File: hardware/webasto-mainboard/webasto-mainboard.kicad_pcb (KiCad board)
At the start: 4 copper layers, 86.8 x 76 mm, 80 parts, among them J1 DEBUG, Q1 DMG2301L, Q10 2N7002, Q11 2N7002, Q12 SSM3J374R, Q13 2N7002, Q14 SUD50P04-08, Q15 SUD50P04-08, Q16 SUD50P04-08, Q17 SUD50P04-08, Q18 SUD50P04-08, Q2 2N7002, Q3 2N7002, Q4 2N7002, Q5 2N7002, Q6 SUD50P04-08, Q7 SUD50P04-08, Q8 SUD50P04-08, Q9 SUD50P04-08, U1 Pico, U2 LM4040DBZ-2.0, U3 LM7805_TO220, U4 MC33660BEFR2, U5 INA219BxDCN, U6 BD9G341EFJ

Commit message: Added logging, added debug serial to mainboard
- also added eeprom read support, and the digital GPIO over I2C
- route the ignition wire as a digital GPIO so we can use it as an input
  to the state machine.
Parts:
- added J1: Console FTDI, Beirdo:FTDI_BASIC, F.Cu at (124.7, 101.9)
- renumbered J1 to J2
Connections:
- U1 pad 24: unconnected-(U1-Pad24) -> ConsoleCTS
- U1 pad 25: unconnected-(U1-Pad25) -> ConsoleRTS
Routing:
- net ConsoleTX: track 0.00 -> 62.9 mm
- net ConsoleRX: track 0.00 -> 61.6 mm, vias 0 -> 1
- net ConsoleRTS: track 0.00 -> 39.8 mm, vias 0 -> 1
- net ConsoleCTS: track 0.00 -> 26.2 mm, vias 0 -> 1
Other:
- board text added: "Webasto Thermo Top C Replacement Controller"
- board text removed: "Webasto Therma Top C Replacement Controller"

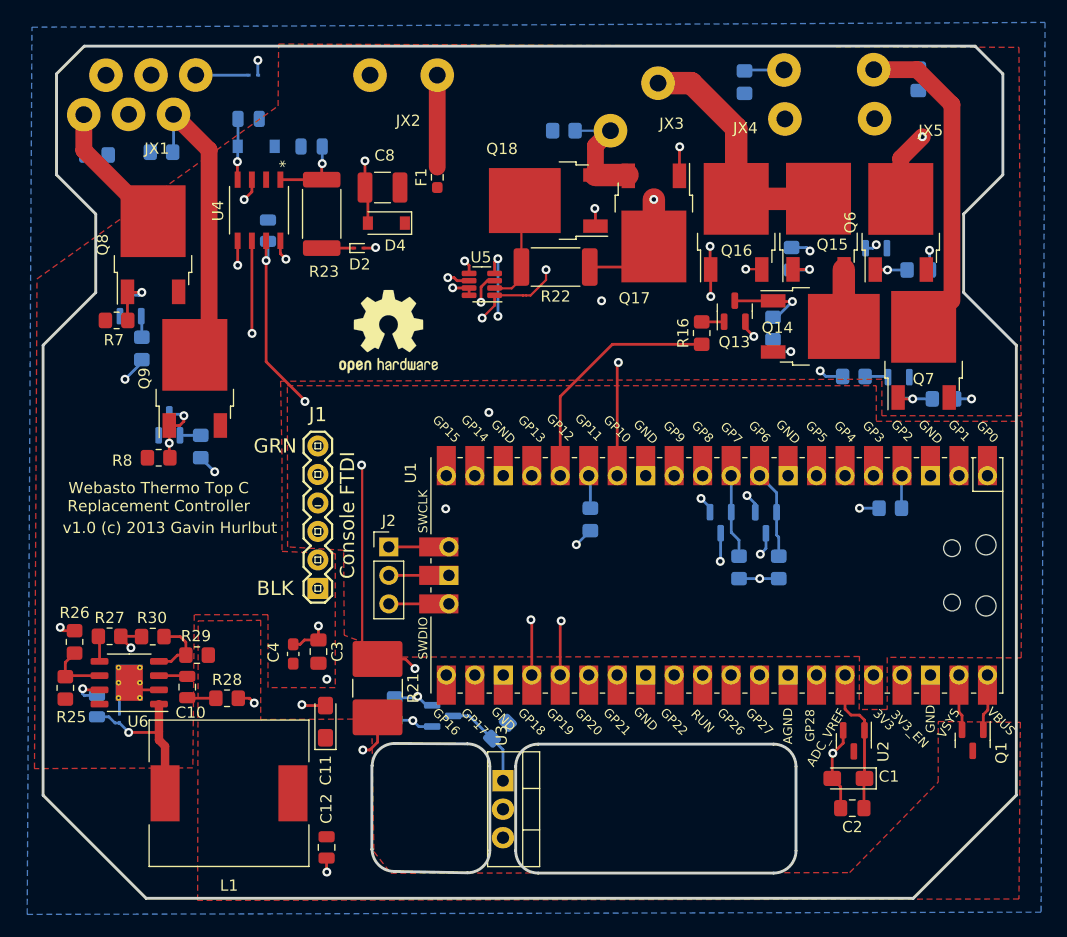
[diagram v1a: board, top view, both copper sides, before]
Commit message: Added a 4kbit FRAM on the mainboard to hold nonvolatile
- things like burn hours.
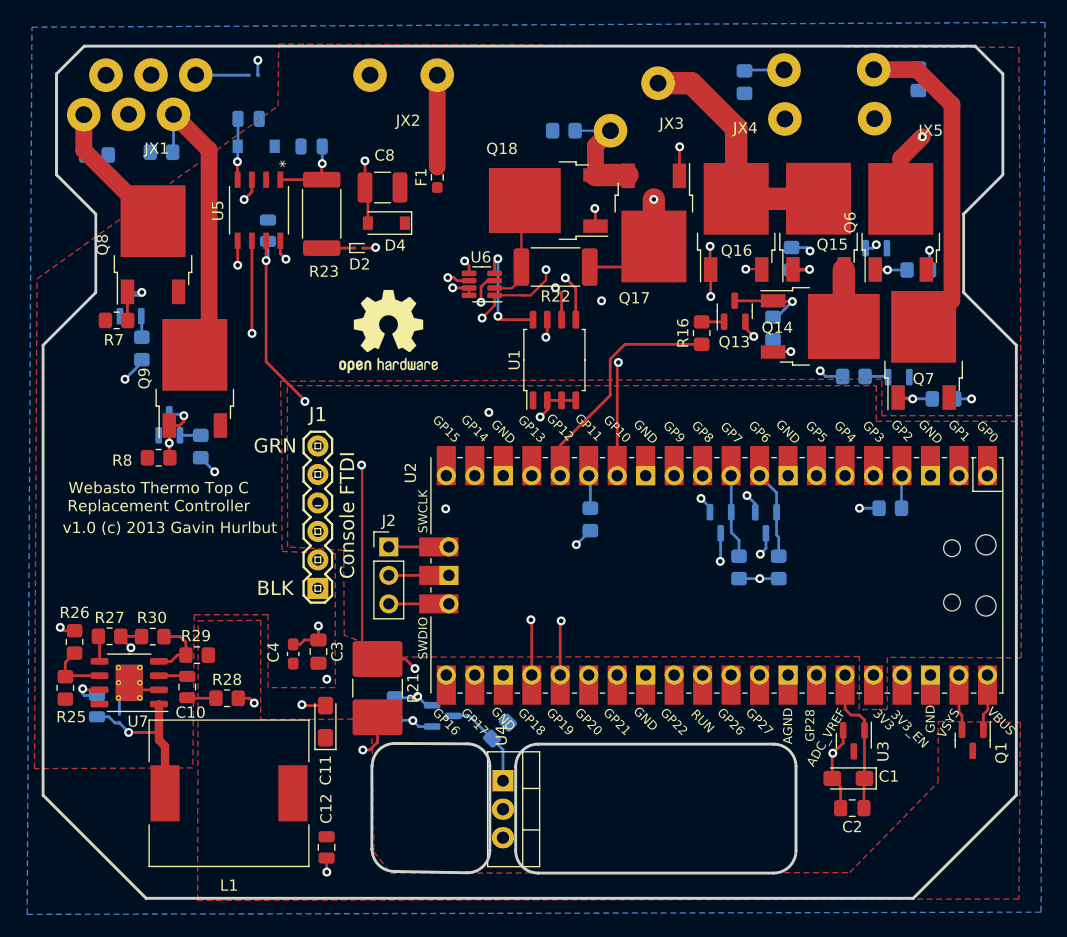
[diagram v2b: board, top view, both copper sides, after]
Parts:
- added U1: CY15E004J, Package_SO:SOIC-8_5.23x5.23mm_P1.27mm, F.Cu at (145.8, 81.5)
- renumbered U1 to U2, U2 to U3, U3 to U4, U4 to U5, U5 to U6, U6 to U7
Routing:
- net GND: track 53.5 -> 59.4 mm, vias 12 -> 14
- net SDA: track 80.6 -> 84.7 mm, vias 1 -> 2
- net +3V3: track 41.7 -> 44.9 mm
- net SCL: track 78.8 -> 81.9 mm, vias 2 -> 3
- net GlowPlugOut3V: track 21.6 -> 20.9 mm

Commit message: Added EmergencyStop input.  Hope I never need it.
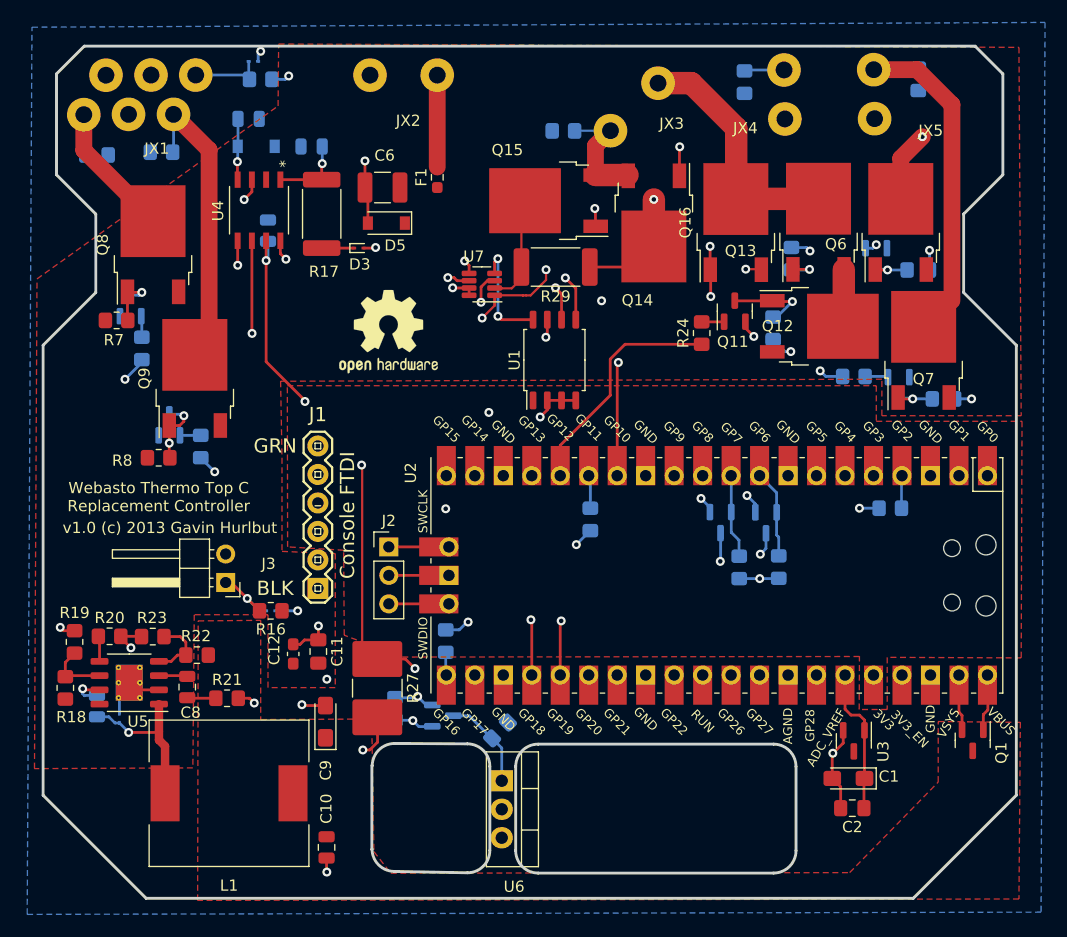
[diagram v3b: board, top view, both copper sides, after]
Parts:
- removed the C3 at (124.8, 107.5)
- removed the C4 at (122.5, 107.8)
- removed the R14 at (162.3, 100.0)
- removed the R17 at (131.6, 112.7)
- removed the R18 at (166.9, 72.5)
- removed the R19 at (140.9, 114.6)
- removed the R20 at (165.3, 78.7)
- removed the R21 at (130.0, 110.8)
- removed the R22 at (145.9, 73.2)
- removed the U4 at (141.2, 119.1)
- added C11: 100nF 25V, Capacitor_SMD:C_0805_2012Metric_Pad1.18x1.45mm_HandSolder, F.Cu at (124.7, 107.5)
- added C12: 100nF 25V, Capacitor_SMD:C_0603_1608Metric_Pad1.08x0.95mm_HandSolder, F.Cu at (122.5, 107.8)
- added D1: ACDBQC0130L-HF, Diode_SMD:D_SOD-923, B.Cu at (120.5, 103.9)
- added J3: 2-pole connector, Connector_PinHeader_2.54mm:PinHeader_1x02_P2.54mm_Horizontal, F.Cu at (116.5, 101.4)
- added R13: 10k, Resistor_SMD:R_0805_2012Metric_Pad1.20x1.40mm_HandSolder, B.Cu at (136.1, 106.6)
- added R25: 10k, Resistor_SMD:R_0805_2012Metric_Pad1.20x1.40mm_HandSolder, B.Cu at (140.9, 114.6)
- added R26: 10k, Resistor_SMD:R_0805_2012Metric_Pad1.20x1.40mm_HandSolder, B.Cu at (165.3, 78.7)
- added R27: 50R 1% 1W, Resistor_SMD:R_2816_7142Metric_Pad3.20x4.45mm_HandSolder, F.Cu at (130.0, 110.8)
- added R28: 100k, Resistor_SMD:R_0805_2012Metric_Pad1.20x1.40mm_HandSolder, B.Cu at (146.6, 61.1)
- added R29: 1R 1% 2W, Resistor_SMD:R_2512_6332Metric_Pad1.40x3.35mm_HandSolder, F.Cu at (145.9, 73.2)
- added R30: 10k, Resistor_SMD:R_0805_2012Metric_Pad1.20x1.40mm_HandSolder, B.Cu at (162.3, 100.0)
- added R31: 10k, Resistor_SMD:R_0805_2012Metric_Pad1.20x1.40mm_HandSolder, B.Cu at (165.8, 100.0)
- added R32: 10k, Resistor_SMD:R_0805_2012Metric_Pad1.20x1.40mm_HandSolder, B.Cu at (131.6, 112.6)
- added R33: 10k, Resistor_SMD:R_0805_2012Metric_Pad1.20x1.40mm_HandSolder, B.Cu at (166.9, 72.5)
- added U7: INA219BxDCN, Package_TO_SOT_SMD:SOT-23-8, F.Cu at (139.3, 74.8)
- Q10: value 2N7002 -> SSM3J374R
- Q11: moved to F.Cu
- Q12: value SSM3J374R -> SUD50P04-08; footprint Package_TO_SOT_SMD:SOT-23 -> Package_TO_SOT_SMD:TO-252-2; moved to F.Cu
- Q13: value 2N7002 -> SUD50P04-08; footprint Package_TO_SOT_SMD:SOT-23 -> Package_TO_SOT_SMD:TO-252-2
- Q17, Q18: value SUD50P04-08 -> 2N7002; footprint Package_TO_SOT_SMD:TO-252-2 -> Package_TO_SOT_SMD:SOT-23; moved to B.Cu
- R16: value 10R -> 10k
- R24: value 100k -> 10R; moved to F.Cu
- U6: value INA219BxDCN -> LM7805_TO220; footprint Package_TO_SOT_SMD:SOT-23-8 -> Package_TO_SOT_THT:TO-220-3_Vertical
- moved R15 63.5 mm to (119.6, 56.5), turned to 180 degrees
- moved Q12 48.3 mm to (169.4, 78.5)
- moved R16 45.7 mm to (120.5, 103.9), turned to 180 degrees
- moved U6 44.3 mm to (141.1, 119.1), turned to -90 degrees
- moved Q18 34.7 mm to (164.7, 96.1), turned to -90 degrees
- moved Q10 30.2 mm to (135.8, 113.2), turned to 0 degrees
- moved Q17 27.4 mm to (160.6, 96.0)
- moved Q15 24.2 mm to (145.3, 67.3), turned to 180 degrees
- moved R24 21.8 mm to (158.9, 79.1), turned to 90 degrees
- moved Q11 19.1 mm to (161.9, 77.2), turned to 90 degrees
- moved Q14 17.5 mm to (154.7, 69.3), turned to -90 degrees
- moved Q13 10.9 mm to (169.3, 69.2)
- moved D2 1.23 mm to (119.0, 54.9)
- renumbered C12 to C10, C5 to C3, C6 to C4, C7 to C5, C8 to C6, C9 to C7, C10 to C8, C11 to C9, D1 to D2, D2 to D3, D3 to D4, D4 to D5, D5 to D6, R13 to R14, R23 to R17, R25 to R18, R26 to R19, R27 to R20, R28 to R21, R29 to R22, R30 to R23, U5 to U4, U7 to U5
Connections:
- Q10 pad 1: +3V3 -> ~{GlowPlugInEN}
- Q10 pad 2: ~{GlowPlugInEN3V} -> +12V
- Q10 pad 3: ~{GlowPlugInEN} -> Net-(Q10-Pad3)
- Q11 pad 1: +3V3 -> Net-(Q11-Pad1)
- Q11 pad 2: ~{GlowPlugOutEN3V} -> GND
- Q11 pad 3: ~{GlowPlugOutEN} -> Net-(Q11-Pad3)
- Q12 pad 1: ~{GlowPlugInEN} -> Net-(Q11-Pad3)
- Q12 pad 2: +12V -> Net-(Q12-Pad2)
- Q12 pad 3: Net-(Q12-Pad3) -> +12V
- Q13 pad 1: Net-(Q13-Pad1) -> ~{GlowPlugOutEN}
- Q13 pad 2: GND -> GlowPlug+
- Q13 pad 3: Net-(Q13-Pad3) -> Net-(Q12-Pad2)
- Q14 pad 1: Net-(Q13-Pad3) -> ~{GlowPlugOutEN}
- Q14 pad 2: Net-(Q14-Pad2) -> GND
- Q14 pad 3: +12V -> GlowPlug-
- Q15 pad 1: ~{GlowPlugOutEN} -> ~{GlowPlugInEN}
- Q15 pad 2: GlowPlug+ -> Kelvin-
- Q15 pad 3: Net-(Q14-Pad2) -> GlowPlug-
- Q17 pad 1: ~{GlowPlugOutEN} -> +3V3
- Q17 pad 2: GND -> ~{GlowPlugInEN3V}
- Q17 pad 3: GlowPlug- -> ~{GlowPlugInEN}
- Q18 pad 1: ~{GlowPlugInEN} -> +3V3
- Q18 pad 2: Kelvin- -> ~{GlowPlugOutEN3V}
- Q18 pad 3: GlowPlug- -> ~{GlowPlugOutEN}
- R15 pad 1: ~{GlowPlugOutEN3V} -> +12V
- R15 pad 2: +3V3 -> StartRun
- R16 pad 1: GlowPlugOut3V -> +12V
- R16 pad 2: Net-(Q13-Pad1) -> EmergencyStop
- R24 pad 1: GlowPlug- -> GlowPlugOut3V
- R24 pad 2: GND -> Net-(Q11-Pad1)
- U2 pad 21: unconnected-(U2-Pad21) -> EmergencyStop3V
- U6 pad 1: Kelvin+ -> Net-(Q10-Pad3)
- U6 pad 2: Kelvin- -> Kelvin+
- U6 pad 3: GND -> Net-(R27-Pad2)
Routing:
- net Net-(R27-Pad2): track 0.00 -> 29.8 mm, vias 0 -> 1
- net Net-(R21-Pad2): track 29.8 -> 0.00 mm, vias 1 -> 0
- net EmergencyStop3V: track 0.00 -> 19.7 mm, vias 0 -> 1
- net Net-(Q12-Pad3): track 8.46 -> 0.00 mm
- net Net-(Q10-Pad3): track 0.00 -> 8.44 mm
- net Net-(Q13-Pad3): track 7.48 -> 0.00 mm, vias 1 -> 0
- net Net-(Q11-Pad3): track 0.00 -> 7.48 mm, vias 0 -> 1
- net EmergencyStop: track 0.00 -> 6.21 mm, vias 0 -> 1
- net Net-(Q14-Pad2): track 5.10 -> 0.00 mm
- net Net-(Q12-Pad2): track 0.00 -> 5.10 mm
- net +3V3: track 44.9 -> 47.2 mm, vias 9 -> 10
- net Net-(Q13-Pad1): track 2.01 -> 0.00 mm
- net Net-(Q11-Pad1): track 0.00 -> 2.01 mm
- net StartRun: track 4.73 -> 6.59 mm
- net +12V: track 21.3 -> 22.9 mm, vias 7 -> 8
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
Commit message: Oops.  StartRun is active at +12V.  Change the level translation.
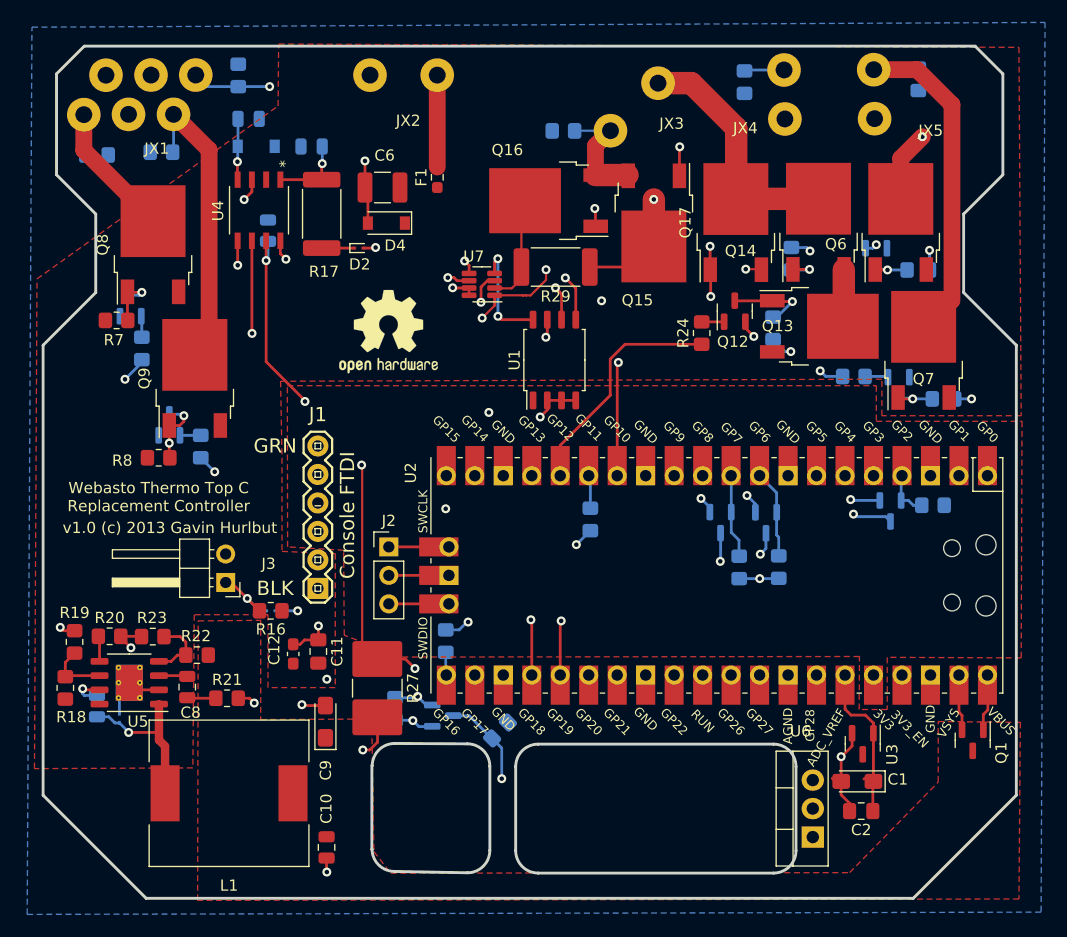
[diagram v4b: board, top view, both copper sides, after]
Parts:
- removed the D2 at (119.0, 54.9)
- added Q10: DMG2301L, Package_TO_SOT_SMD:SOT-23, B.Cu at (175.8, 95.0)
- moved U6 28.2 mm to (168.8, 124.1), turned to 90 degrees
- moved R15 3.82 mm to (179.6, 94.5)
- moved R14 2.03 mm to (117.6, 56.1), turned to 90 degrees
- moved C1 0.84 mm to (172.8, 119.1)
- moved U3 0.84 mm to (173.3, 115.8)
- moved C2 0.84 mm to (173.2, 121.8)
- renumbered D3 to D2, D4 to D3, D5 to D4, D6 to D5, Q10 to Q11, Q11 to Q12, Q12 to Q13, Q13 to Q14, Q14 to Q15, Q15 to Q16, Q16 to Q17, Q17 to Q18, Q18 to Q19, R15 to R14, R14 to R15
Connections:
- net EmergencyStop3V renamed ~{EmergencyStop3V}
- D1 pad 1: EmergencyStop -> ~{EmergencyStop}
- R14 pad 1: +12V -> StartRun
- R14 pad 2: StartRun -> GND
- R15 pad 1: +3V3 -> ~{StartRun3V}
- R15 pad 2: StartRun3V -> GND
- R16 pad 2: EmergencyStop -> ~{EmergencyStop}
- U2 pad 4: StartRun3V -> ~{StartRun3V}
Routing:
- net StartRun3V: track 99.1 -> 0.00 mm, vias 1 -> 0
- net StartRun: track 6.59 -> 97.3 mm, vias 0 -> 2
- net Net-(Q11-Pad3): track 8.44 -> 48.1 mm, vias 0 -> 1
- net Kelvin+: track 83.2 -> 112.5 mm
- net Net-(R27-Pad2): track 29.8 -> 47.5 mm
- net ~{EmergencyStop}: track 0.00 -> 6.21 mm, vias 0 -> 1
- net EmergencyStop: track 6.21 -> 0.00 mm, vias 1 -> 0
- net ~{StartRun3V}: track 0.00 -> 4.41 mm
- net +3V3: track 47.2 -> 49.2 mm
- net +12V: track 22.9 -> 21.3 mm, vias 8 -> 7
- net GND: track 59.4 -> 60.5 mm
- net /ADC_VREF: track 13.0 -> 13.9 mm

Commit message: Added the LEDs onto the board and init
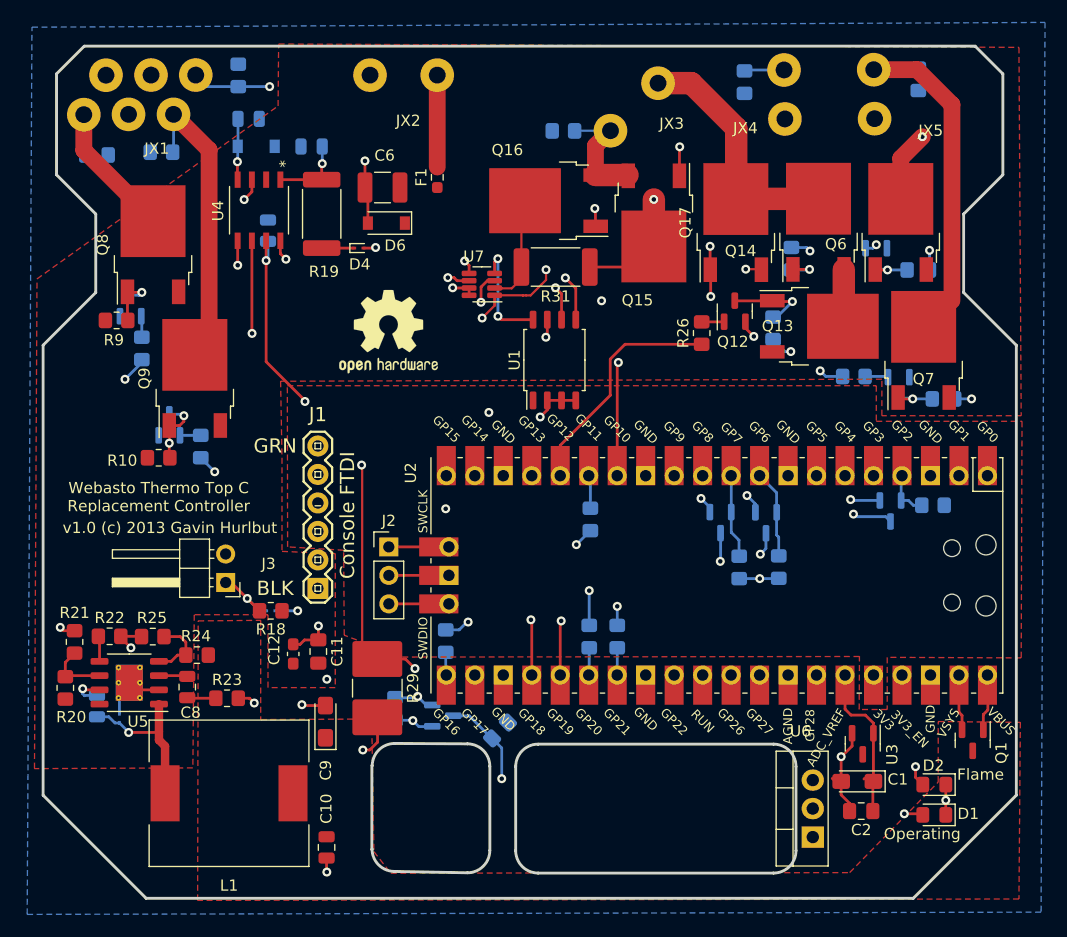
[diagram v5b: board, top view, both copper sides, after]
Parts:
- added D1: LED, LED_SMD:LED_0805_2012Metric_Pad1.15x1.40mm_HandSolder, F.Cu at (179.7, 122.1)
- added D2: LED, LED_SMD:LED_0805_2012Metric_Pad1.15x1.40mm_HandSolder, F.Cu at (179.7, 119.4)
- added R1: 1k, Resistor_SMD:R_0805_2012Metric_Pad1.20x1.40mm_HandSolder, B.Cu at (151.4, 106.2)
- added R2: 1k, Resistor_SMD:R_0805_2012Metric_Pad1.20x1.40mm_HandSolder, B.Cu at (148.9, 106.2)
- renumbered D1 to D3, D2 to D4, D3 to D5, D4 to D6, D5 to D7, R8 to R10, R9 to R11, R10 to R12, R11 to R13, R12 to R14, R13 to R15, R14 to R16, R15 to R17, R16 to R18, R17 to R19, R18 to R20, R19 to R21, R20 to R22, R21 to R23, R22 to R24, R23 to R25, R24 to R26, R25 to R27, R26 to R28, R27 to R29, R1 to R3, R28 to R30, R29 to R31, R30 to R32, R31 to R33, R32 to R34, R33 to R35, R2 to R4, R3 to R5, R4 to R6, R5 to R7, R6 to R8, R7 to R9
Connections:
- U2 pad 26: unconnected-(U2-Pad26) -> FlameLED
- U2 pad 27: unconnected-(U2-Pad27) -> OperatingLED
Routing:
- net Net-(D2-Pad2): track 0.00 -> 46.0 mm, vias 0 -> 2
- net Net-(D1-Pad2): track 0.00 -> 38.7 mm, vias 0 -> 2
- net GND: track 60.5 -> 63.2 mm, vias 14 -> 15
- net FlameLED: track 0.00 -> 2.45 mm
- net OperatingLED: track 0.00 -> 2.43 mm
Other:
- board text added: "Flame"
- board text added: "Operating"
